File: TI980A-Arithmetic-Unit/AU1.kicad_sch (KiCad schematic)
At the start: 245 parts, among them J1 Circuit Type Test, J2 Circuit Type Test, U1 7413N, U10 74H04N, U100 7410N, U101 7474N, U102 74H52N, U103 74163, U104 7408N, U105 74H11N, U106 74H52N, U107 7451N, U108 74H52N, U109 7404N, U11 74H04N, U110 74H11N, U111 7410N, U112 7420N, U113 7400N, U114 74H54W, U115 7410N, U116 74H11N, U117 74H04N, U118 74H21N, U119 74H52N, U12 74LS74, U120 74188N, U121 74H11N, U122 74157N, U123 7404N, U124 74H11N, U125 74H51N, U126 74H01N, U127 7410N, U128 7474N, U129 7400N, U13 74H00N, U130 74H01N, U131 74H52N, U132 74H05N, U133 74H22N, U134 7410N, U135 7451N, U136 7420N, U137 7427N, U138 74S22N, U139 74S65N, U14 74H10, U140 74H52N, U141 74H52N, U142 74175N, U143 74175N, U144 74H52N, U145 74187, U146 74187, U147 74H52N, U148 74H61N, U149 74H61N, U150 74H61N, U151 7451N, U152 74H61N, U153 74S22N, U154 74H30N, U155 74187, U156 74H04N, U157 74187, U158 74H61N, U159 74H61N, U160 7451N, U161 74H61N, U162 74H61N, U163 74H61N, U164 74H61N, U165 74LS83, U166 74H30N, U167 74H11N, U168 7402N, U169 74H103N, U170 7400N, U171 7402N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

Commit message: Finished Adding Every Chip and Net label in AU1
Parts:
- removed U36: 7402N, symbol 74xx:7402
- removed U76: 7410N, symbol 74xx:74LS10
- added C3, C4: C_Polarized, symbol Device:C_Polarized
- added R49, R50, R51, R52, R54, R55, R56, R73, R74, R75, R76, R78, R79, R80: R, symbol Device:R
- added R53, R77: ~, symbol Device:R
- added U185, U187, U203, U207, U213, U226, U227: 7404N, symbol 74xx:74LS04
- added U186: 74154, symbol 74xx_IEEE:74154
- added U188, U202: 7402N, symbol 74xx:7402
- added U189, U190, U212: 7474N, symbol 74xx:74LS74
- added U191, U204, U217, U218, U220, U224: 7400N, symbol 74xx:7400
- added U192, U199, U208: 7430N, symbol 74xx:74LS30
- added U193, U210, U216, U225: 7420N, symbol 74xx:74LS20
- added U194, U195: 74H21N, symbol 74xx:74LS21
- added U196, U197, U205, U209, U211: 74H54W, symbol TI980A:74H54N
- added U198, U200: 7410N, symbol 74xx:74LS10
- added U201, U36: 74S22N, symbol 74xx:74LS22
- added U206: 7451N, symbol TI980A:7451N
- added U214: 7486N, symbol 74xx:74LS86
- added U215: 74S65N, symbol TI980A:74S65N
- added U219, U221, U223: 74H52N, symbol TI980A:74H52N
- added U222: 7408N, symbol 74xx:74LS08
- added U228: 74S10N, symbol 74xx:74LS10
- added U76: 74H00N, symbol 74xx:7400
- R11: Location AU1 Column 10 Row 05 -> AU1 Col 10 Row 05
- R17, R18, R20, R24, R25: Location AU1 Column 2 Row 09 -> AU1 Col 2 Row 09
- R23: Location AU1 Column 3 Row 01 -> AU1 Col 3 Row 01
- R36: Location AU1 Column 4 Row 12 -> AU1 Col 4 Row 12
- U89: Location AU1 COlumn 13 Row 13 -> AU1 Column 13 Row 13
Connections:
- net AR0XAR2 is gone; now on net ~{AR0XAR2}: U83.11
- net C8OP is gone; now on net C80P: R12.2, U105.1
- net MBL3PA1 is gone; now on net M8L3PA1: U98.13
- net MBl2J2 is gone; now on net MBL2J2: U116.8
- net MCL4P4 is gone; now on net MCL4PA: U124.12
- net ~{AR14XIR9} is gone; now on net ~{AP14XIR9}: U109.6
- net ~{INTRTOPA} is gone; now on net ~{INSRTOPA}: R35.2
- net ~{M8LCPA} is gone; now on net ~{MBLCPA}: U111.8
- net ~{M8LEJ2} is gone; now on net ~{M8LEJ1}: U86.6
- net ~{MAL8AA} is gone; now on net ~{MAL8APA}: U129.3
- net ~{MEM0A} is gone; now on net ~{MEM0}: U24.13
- net ~{ST5T} is gone; now on net ST5T: U109.2
- net A0XA1: now also U207.13
- net ADRV: now also U227.4
- net AL0E1U0: now also U51.6
- net ALU0T: now also U182.9, U51.3, U91.9, U215.4, U36.4
- net ALUEQ8K: now also U182.2
- net AR0: now also U214.1, U215.11
- net AR0XAR1: now also U206.10
- net AR1: now also U214.13
- net AR15: now also U217.9
- net AR1XIR9: now also U214.11
- net AU2CLK: now also U75.9; no longer U21.9
- net BFR0: now also U182.5
- net BFR6: now also U52.3
- net C80P: now also U4.4, U224.2
- net CFZ: now also U26.4
- net CLKONQ: now also U51.9
- net CYCOMP: now also U228.5
- net DMAQ: now also U212.9 (Q)
- net DMARECD: now also U195.8
- net ECEK: now also U58.10
- net ENPCOUT: now also U11.13
- net ER1: now also U51.4, U91.10
- net ER14: now also U194.12
- net ER15: now also U11.11
- net EXEJ: now also U58.4
- net EXPQ: now also U181.9 (Q)
- net EXRCEQ: now also U181.5 (Q)
- net EXRECD: now also U181.2 (D)
- net FCLKT: now also U23.11, U24.6; no longer U23.10, U23.6, U24.11, U24.5
- net FORALA: now also U190.2 (D)
- net FORCE00: now also U29.4
- net FSWON: now also U211.1
- net GCLKE:1: now also U76.13, U76.5
- net GND: now also U179.12 (GND), U179.18 (~{E0}), U179.19 (~{E1}), U186.12 (GND), U186.18 (~{E0}), U186.19 (~{E1}), U196.4, U196.5, U196.6, U205.4, U205.5, U205.6, U215.2, U215.3
- net ILLOPA: now also U76.3
- net ILOPQ: now also U195.1
- net IMM: now also U207.10
- net INAQ: now also U11.1
- net INSRTOP: now also U26.10
- net INTINT: now also U64.9, U91.3
- net INTM: now also U29.12
- net INTST: now also U187.3, U188.13
- net IOINT: now also U227.6
- net IR11: now also U48.5
- net IR5: now also U218.9, U228.9
- net IR56BSD: now also U37.4
- net IR8: now also U37.10
- net IR8T: now also U208.2
- net IR911: now also U48.6, U215.9
- net IR9T: now also U48.4, U213.9, U214.12, U214.2
- net L0: now also U203.4, U211.13, U217.10, U222.13
- net L1: now also U44.2, U197.13, U206.13, U206.3, U211.6, U218.13, U220.2
- net L2: now also U21.3, U193.13, U197.3, U198.13, U222.5, U228.4
- net L23: now also U204.3
- net L2467: now also U225.6
- net L3: now also U184.13, U29.10, U195.13, U197.10, U211.3
- net L4: now also U3.8, U69.11, U74.11, U193.5, U194.13, U197.6, U200.13, U222.2, U224.13
- net L5: now also U185.12, U206.4, U206.9, U209.13, U210.5, U211.10
- net L56: now also U64.6
- net L567: now also U37.9
- net L6: now also U184.5, U200.11, U207.6, U209.3
- net L7: now also U207.4, U209.10, U210.13, U218.10, U224.5
- net L8: now also U209.6
- net L8A: now also U204.8
- net L9: now also U50.5, U77.5, U187.12
- net L9D: now also U77.3
- net LA: now also U185.8
- net LB: now also U200.5, U203.12
- net LC: now also U213.12, U220.10
- net LD: now also U176.4
- net LE: now also U37.5, U185.6, U228.11
- net LF: now also U187.10, U195.5, U196.9
- net M0: now also U75.6, U195.12, U196.13, U196.2, U221.3, U223.3
- net M0L0J3: now also U223.4
- net M0OP: now also U196.1
- net M1: now also U176.10, U221.12, U223.12
- net M3: now also U220.1, U223.1
- net M3L1CJ3: now also U223.2
- net M3L567J1: now also U37.8
- net M5: now also U176.12, U219.3, U221.10
- net M67910: now also U4.1
- net M7: now also U187.8, U196.10
- net M7L3: now also U188.10
- net M8: now also U75.3, U205.10, U221.1
- net M8LB: now also U178.1, U201.9
- net M8LBC: now also U91.13
- net MA: now also U21.8, U219.12
- net MALEFJ3: now also U219.13
- net MB: now also U203.2, U219.10
- net MC: now also U203.10, U228.3
- net MCJ1: now also U224.8
- net MCL3: now also U183.13
- net MD: now also U185.2, U205.3
- net MDJ1: now also U199.8
- net MDPA1: now also U192.8
- net ME: now also U176.8, U44.1
- net MEL3: now also U202.4
- net MEM0PA1: now also U113.8; no longer U98.4
- net MEM10A: now also U24.10
- net MEM12: now also U26.6, U228.2
- net MEM5A: now also U4.2, U198.3
- net MEM6: now also U23.5
- net MEM6A: now also U198.4
- net MEM7A: now also U198.5
- net MEM8A: now also U29.6, U220.9
- net MFLC: now also U188.1
- net MFM0PA1: now also U98.4; no longer U113.8
- net MRESETQ: now also U222.12
- net R22: now also U216.10
- net RAC0: now also U186.20 (A3)
- net RAC1: now also U186.21 (A2)
- net RAC2: now also U186.22 (A1)
- net RAC3: now also U186.23 (A0)
- net RAC4: now also U179.20 (A3)
- net RAC5: now also U179.21 (A2)
- net RAC6: now also U179.22 (A1)
- net RAC7: now also U179.23 (A0)
- net RDYIO: now also U227.10
- net RR: now also U228.1
- net RUNFFQ: now also U50.1, U197.1, U216.12
- net SC0: now also U91.2, U213.1
- net SC2: now also U48.10
- net SC3: now also U48.9, U222.9
- net SC3B: now also U222.8
- net SCNT06: now also U48.8
- net SCNT0F: now also U220.5
- net SCNT1E: now also U222.1, U222.4
- net SELBFR: now also U52.2
- net SELBFRB: now also U224.1
- net SELBFRC: now also U183.9, U76.4
- net SELJ3: now also U183.6
- net SELJ3A: now also U223.8
- net SELJ3B: now also U219.8
- net SELPAA: now also U221.8
- net TRP13Q: now also U195.9, U212.5 (Q)
- net TRP1413: now also U52.12
- net TRP14Q: now also U189.9 (Q), U195.2
- net UR0: now also U51.5, U91.11, U213.3
- net VCC1: now also U179.24 (VCC), U180.11, U180.12, U180.6, U181.1 (~{R}), U181.10 (~{S}), U181.13 (~{R}), U181.4 (~{S}), U183.10, U183.4, U21.2, U3.10, U52.1, U75.10, U75.2, U75.5, U77.12, U91.5, C3.1, C4.1, R49.1, R50.1, R51.1, R52.1, R53.1, R54.1, R55.1, R56.1, R73.1, R74.1, R75.1, R76.1, R77.1, R78.1, R79.1, R80.1, U186.24 (VCC), U189.1 (~{R}), U189.10 (~{S}), U189.13 (~{R}), U189.4 (~{S}), U190.1 (~{R}), U190.4 (~{S}), U191.1, U197.4, U199.12, U208.11, U209.4, U212.1 (~{R}), U212.10 (~{S}), U212.13 (~{R}), U212.4 (~{S}), U215.13, U219.5, U221.5, U222.10, U223.5
- net XRDSW: now also U45.6, U209.5
- net ~{A0XA1}: now also U74.9, U207.12
- net ~{ADRV}: now also U227.3
- net ~{ALU0T}: now also U182.8, U201.12, U201.4, U215.1
- net ~{ALUEQ8K}: now also U182.1
- net ~{AR0T}: now also U215.5
- net ~{ARDSW}: now also U184.10, U47.3
- net ~{ARESW}: now also U184.9, U207.1
- net ~{BFR0}: now also U182.6
- net ~{BRDSW}: now also U45.11, R50.2, U193.1, U200.1
- net ~{BRESW}: now also U184.12
- net ~{CLCNT}: now also U225.8
- net ~{CNT}: now also U225.10
- net ~{DEVTHERE}: now also U183.1
- net ~{DMAINT}: now also R75.2, U226.13
- net ~{DMAM}: now also U204.12, U216.2
- net ~{E14XE15}: now also U69.9
- net ~{ENAPI1}: now also U228.6
- net ~{ENIOUT}: now also U51.8
- net ~{ENPCOUT}: now also U11.12, U51.10
- net ~{ERDSW}: now also R54.2, U193.2
- net ~{ERESW}: now also U47.5, R56.2, U193.4
- net ~{EXPINT}: now also U47.13
- net ~{EXPM}: now also U194.4, U216.1
- net ~{FCLKT}: now also U24.5; no longer U23.5, U24.6
- net ~{FORCE00}: now also U183.3, U183.5, U29.3
- net ~{GCLKF:1}: now also U190.3 (C)
- net ~{GCLKF:2}: now also U181.11 (C), U181.3 (C), U189.3 (C)
- net ~{GCLKF:3}: now also U75.8; no longer U21.8
- net ~{IAQBFR}: now also U216.8
- net ~{IFLAGQ}: now also U91.4
- net ~{INAQ}: now also U11.2, U64.10, U194.1, U216.5, U76.10
- net ~{INSRTOPA}: now also U26.8
- net ~{INTABORT}: now also U226.9
- net ~{INTM}: now also U29.13, U216.13
- net ~{IOINT}: now also R76.2, U227.5
- net ~{IOM}: now also U203.5, U204.13
- net ~{IR10}: now also U208.12
- net ~{IR5T}: now also U208.5
- net ~{IR6T}: now also U208.4, U228.10
- net ~{IR7T}: now also U208.3
- net ~{IR9T}: now also U205.13, U208.1, U213.8
- net ~{IRDSW}: now also U45.9, R51.2, U193.9, U198.1
- net ~{L01}: now also U58.6
- net ~{L0}: now also U179.1 (~{S0}), U74.4, U203.3
- net ~{L1}: now also U179.2 (~{S1}), U58.9
- net ~{L2}: now also U179.3 (~{S2}), U180.1, U21.1, U204.1, U225.1
- net ~{L3}: now also U179.4 (~{S3}), U180.2, U29.11, U188.9, U202.6, U204.2
- net ~{L4}: now also U178.6, U179.5 (~{S4}), U180.3, U3.9, U69.1, U74.5, U225.4
- net ~{L5}: now also U179.6 (~{S5}), U180.4, U64.5, U69.2, U185.13
- net ~{L6}: now also U179.7 (~{S6}), U180.5, U64.4, U69.13, U207.5, U225.2
- net ~{L7}: now also U179.8 (~{S7}), U207.3, U225.5
- net ~{L8}: now also U179.9 (~{S8}), U188.6, U204.9, U217.1
- net ~{LA}: now also U179.11 (~{S10}), U185.9, U204.10, U204.4
- net ~{LB}: now also U178.2, U179.13 (~{S11}), U202.12, U203.13, U204.5
- net ~{LC}: now also U179.14 (~{S12}), U58.3, U188.3, U213.13
- net ~{LDSC}: now also U224.3, U225.9
- net ~{LE}: now also U178.12, U179.16 (~{S14}), U185.5, U217.2
- net ~{LF}: now also U179.17 (~{S15}), U187.11, U188.12
- net ~{LRACLR}: now also U44.3
- net ~{LRDSW}: now also R77.2, U210.2, U227.13
- net ~{LRESW}: now also R52.2, U210.1, U226.1
- net ~{M0L4BFR}: now also U77.11
- net ~{M0LEJ1}: now also U228.8
- net ~{M0}: now also U178.5, U75.4, U186.1 (~{S0})
- net ~{M1}: now also U176.11, U186.2 (~{S1})
- net ~{M2}: now also U186.3 (~{S2}), U203.9
- net ~{M3}: now also U186.4 (~{S3})
- net ~{M4}: now also U186.5 (~{S4})
- net ~{M5L2PA}: now also U217.5
- net ~{M5}: now also U176.13, U186.6 (~{S5})
- net ~{M6}: now also U186.7 (~{S6}), U202.11
- net ~{M8L0J1}: now also U217.8
- net ~{M8L2PA}: now also U220.12
- net ~{M8L456J1}: now also U202.1
- net ~{M8LEJ1}: now also U218.5
- net ~{M8}: now also U178.3, U58.2, U186.9 (~{S8})
- net ~{MAESW}: now also U47.1
- net ~{MALCPA1}: now also U220.8
- net ~{MALEBFR}: now also U50.12
- net ~{MA}: now also U178.11, U21.9, U186.11 (~{S10}), U216.9
- net ~{MBL6CJ3}: now also U213.5
- net ~{MBLA8PA}: now also U218.3
- net ~{MB}: now also U178.8, U186.13 (~{S11}), U203.1
- net ~{MCLDJ1}: now also U224.10
- net ~{MC}: now also U186.14 (~{S12}), U203.11
- net ~{MDDSW}: now also U45.3, R55.2, U191.4
- net ~{MDESW}: now also U44.4
- net ~{MDIDSW}: now also U191.5
- net ~{MDIESW}: now also U44.5
- net ~{MDL1PA1}: now also U192.1
- net ~{MDL8PA1}: now also U192.12
- net ~{MD}: now also U58.8, U185.1, U186.15 (~{S13})
- net ~{MEM10}: now also U24.11
- net ~{MEM11}: now also U187.1
- net ~{MEM15}: now also U226.5
- net ~{MEM6}: now also U23.6
- net ~{MEM8}: now also U29.5
- net ~{ME}: now also U176.9, U58.5, U186.16 (~{S14}), U202.5
- net ~{MF}: now also U186.17 (~{S15}), U187.5, U188.11, U188.2, U188.5
- net ~{MRDSW}: now also U184.1, U191.2
- net ~{MRESW}: now also R80.2, U210.4
- net ~{OVRST}: now also U208.8
- net ~{PCDSW}: now also R49.2, U193.10
- net ~{PCESW}: now also U45.13, U193.12
- net ~{R19}: now also U51.11
- net ~{RDYIO}: now also R74.2, U227.11
- net ~{RRDESZ}: now also U26.5, U228.13
- net ~{RSTSW}: now also U227.1
- net ~{RUNFFQ}: now also U211.4
- net ~{SCNT0F}: now also U69.10, U194.9
- net ~{SCNT1E}: now also U74.10, U74.3, U218.12, U218.2
- net ~{SELBFRCK}: now also U76.6
- net ~{SELJ1}: now also U215.8
- net ~{SELJ2B}: now also U205.8
- net ~{SELJ2C}: now also U91.12
- net ~{SELJ3}: now also U183.2
- net ~{SELOP}: now also U196.8
- net ~{SELPA}: now also U201.6, U201.8, U36.6
- net ~{SRDSW}: now also R73.2, U210.10, U226.3
- net ~{SRESW}: now also R78.2, U210.9, U226.11
- net ~{STDSW}: now also U184.2
- net ~{STESW}: now also U184.4, U47.9
- net ~{STRTSW}: now also R53.2
- net ~{SYSCLK}: now also U23.10; no longer U23.11, U24.10
- net ~{T2OR6}: now also U176.2
- net ~{T4OR6}: now also U176.6
- net ~{TRP13}: now also U195.4
- net ~{UR0T}: now also U201.5, U213.11, U213.4
- net ~{XRDSW}: now also U45.5, U200.3
- net ~{XRESW}: now also R79.2, U210.12
- net EXPINT: now reaches U181.12 (D)
- net EXPINT: now also U47.12
- net ~{EXPQ}: now reaches U181.8 (~{Q})
- net M0LEOP: now reaches U37.6
- net M0LEOP: now also U196.3
- net M8LC: now reaches U58.1
- net M8LC: now also U201.1, U36.1
- net T4OP6: now reaches U176.5
- net T4OP6: now also U194.6, U212.2 (D)
- net ~{ER15T}: now reaches U11.10
- net ~{ER15T}: now also U194.10
- net ~{M8L4PA}: now reaches U69.8
- net ~{M8L4PA}: now also U220.13
- net ~{M1L4PA}: now reaches U74.8
- net ~{M1L4PA}: now also U191.9
- net ~{MDL3PA1}: now reaches U184.8
- net ~{MDL3PA1}: now also U192.3
- net ERESW: now reaches U47.6
- net ERESW: now also U200.2
- net L456: now reaches U69.12
- net L456: now also U220.4
- net ~{AL0E1U0}: now reaches U91.8
- net ~{AL0E1U0}: now also U91.1
- net M0L4: now reaches U178.4
- net M0L4: now also U77.13
- net ~{MDL6PA1}: now reaches U184.6
- net ~{MDL6PA1}: now also U192.6
- net ~{INTINT}: now reaches U91.6
- net ~{INTINT}: now also U50.2, U194.2
- net MDE: now reaches U44.6
- net MDE: now also U77.4, U185.3
- net ~{MDL9J2}: now reaches U77.6
- net ~{MDL9J2}: now also U198.11
- net ~{LD}: now reaches U176.3
- net ~{LD}: now also U178.9, U179.15 (~{S13}), U77.2
- net MEM11A: now reaches U4.5
- net MEM11A: now also U187.2
- net ~{ILLSKIP}: now reaches U4.6
- net ~{ILLSKIP}: now also U76.2
- net T20R6: now reaches U176.1
- net T20R6: now also U189.12 (D), U217.11
- net MBLD: now reaches U178.10
- net MALE: now reaches U178.13
- net MALE: now also U50.13
- net ~{IMM}: now reaches U26.9
- net ~{IMM}: now also U198.6, U207.11
- net ARDSW: now reaches U47.4
- net ARDSW: now also U211.2
- net STESW: now reaches U47.8
- net STESW: now also U200.10
- net at U138.2, U62.13: now also U201.10, U201.2, U213.2, U36.2
- net ~{MDE}: now reaches U50.3
- net ~{MDE}: now also U185.4
- net MDDID: now reaches U50.4
- net MDDID: now also U191.6
- net ~{MDL9J1}: now reaches U50.6
- net ~{MDL9J1}: now also U199.11
- net L23456: now reaches U180.8
- net MDDSW: now reaches U45.4
- net ~{ILOPD}: now reaches U183.8
- net ~{ILOPD}: now also U29.9
- net ~{M1PAA}: now reaches U74.6
- net ~{M1PAA}: now also U191.10
- net MAESW: now reaches U47.2
- net MAESW: now also U200.4
- net PCESW: now reaches U45.12
- net PCESW: now also U198.2
- net ILOPD: now reaches U29.8
- net ILOPD: now also U189.2 (D)
- net ~{L9}: now reaches U179.10 (~{S9})
- net ~{L9}: now also U77.1, U187.13
- net BRDSW: now reaches U45.10
- net BRDSW: now also U197.5
- net ~{EXRECQ}: now reaches U181.6 (~{Q})
- net ~{INT14A}: now reaches U64.8
- net ~{INT14A}: now also U217.12
- net ~{M9}: now reaches U75.1
- net ~{M9}: now also U185.11, U186.10 (~{S9})
- net IRDSW: now reaches U45.8
- net IRDSW: now also U197.2
- net L8F renamed L8E
- net L8E: now also U217.3
- new net AR0XIR9: U206.1, U214.3
- new net ARESW: U197.9, U207.2
- new net DMAINT: U212.12 (D), U226.12
- new net DMAIO: U194.5, U204.11
- new net FORALAQ: U190.5 (Q), U208.6
- new net GND1: C3.2, C4.2
- new net INOPQ: U189.5 (Q)
- new net INTABORT: U224.12, U226.8
- new net INTIAQ: U76.12, U76.8
- new net IOM: U203.6, U216.4
- new net LAB: U204.6, U218.1
- new net LRDSW: U211.9, U227.12
- new net LRESW: U209.1, U226.2
- new net M0L0PA: U221.4, U222.11
- new net M1L4J3: U222.3, U223.13
- new net M1PA: U191.8, U221.13
- new net M2: U203.8, U206.2, U206.5, U223.10
- new net M2L15J3: U207.8, U223.11
- new net M5L12PA: U217.6, U221.11
- new net M5L2J3: U219.4, U222.6
- new net M6LB: U202.13, U215.12, U215.6
- new net M8J2: U205.9, U218.6
- new net M8L24PA: U220.11, U221.2
- new net M8L4J1: U194.8, U202.2
- new net M8L56J1: U202.3
- new net M9: U185.10
- new net MBL6CJ3: U213.6, U219.11
- new net MDJ2: U198.8, U205.2
- new net MEM15A: U226.6
- new net MF: U187.6, U219.1
- new net MFL8: U188.4, U205.1, U215.10
- new net MFLFJ3: U195.6, U219.2
- new net MRDSW: U191.3, U209.2
- new net RSTSW: U211.5, U227.2
- new net SRDSW: U224.4, U226.4
- new net SRESW: U209.9, U226.10
- new net UR0T: U201.13, U213.10, U36.5
- new net ~{DMAQ}: U212.8 (~{Q})
- new net ~{FORALAQ}: U190.6 (~{Q})
- new net ~{GCLHF:3}: U212.11 (C)
- new net ~{INOPQ}: U189.6 (~{Q})
- new net ~{INT14B}: U216.6, U217.13
- new net ~{INTST}: U187.4, U76.9
- new net ~{M2L15J3}: U206.8, U207.9
- new net ~{M2L15}: U206.6, U225.12
- new net ~{M3L1}: U220.3, U225.13
- new net ~{M5L1PA}: U217.4, U218.11
- new net ~{M7}: U186.8 (~{S7}), U187.9, U188.8
- new net ~{M8J2A}: U218.4, U220.6
- new net ~{MCL4J1}: U224.11, U224.9
- new net ~{MDJ1A}: U199.1, U211.8
- new net ~{MDJ2A}: U197.8, U198.9
- new net ~{MDJ2B}: U198.10, U209.8
- new net ~{MDL2J1}: U198.12, U199.2
- new net ~{MDL2PA1}: U192.2, U193.8
- new net ~{MDL4J1}: U199.3, U200.12
- new net ~{MDL4PA1}: U192.4, U193.6
- new net ~{MDL5PA1}: U192.5, U210.6
- new net ~{MDL6J1}: U199.4, U200.8
- new net ~{MDL7J1}: U199.5, U218.8, U224.6
- new net ~{MDL7PA1}: U192.11, U210.8
- new net ~{MDL8J1}: U199.6, U200.6
- new net ~{RRILLOP}: U228.12, U76.1
- new net ~{TRP13Q}: U212.6 (~{Q})
- new net ~{TRP14Q}: U189.8 (~{Q}), U195.10
- new net ~{TRPCLK}: U189.11 (C), U212.3 (C), U76.11
- no-connect marks 161 -> 195
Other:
- note added: "BFR(0-7) Signals Used as Next ROM Address for SELBFR"
- note added: "BFR0 = BFR0 ROM Output"
- note added: "Basic Function ROM (BFR) The 32x8 Word Rom in the BFR Logic Decodes Bsic Information about an Instruction Being Fetched"
- note added: "Branch, Store or Double Instuction Flag"
- note added: "Clock Enabled During SELBFR"
- note added: "DBL"
- note added: "Denotes Byte Inst. In Process"
- note added: "Double Length Instruction Flag"
- note added: "Expansion Interrupt Recognized"
- note added: "Forces BFR(4-7) to Zero for Shift Inst. with C Field=0"
- note added: "INTERUPT LOGIC"
- note added: "IXB Field = 111"
- note added: "Illegal OP Code Flag"
- note added: "Illegal Skip or RR Instruction"
- note added: "MEMORY DATA BUFFERING"
- note added: "Masked DMA Interrupt"
- note added: "Masked I/O Interrupt"
- note added: "Next ROM Address Selector Select J2 (~{SELJ2})"
- note added: "RR Instruction with Illegal Destination"
- note added: "RR Interrupt Inhibit (When DEST = ST)"
- note added: "Select J3 as Next ROM Address (SELJ3)"
- note added: "Select Present Address + 1 as Next ROM Address (~{SELPA1})"
- note added: "Select Present ROM Address as the Next ROM Address"
- note added: "Syncronized DMA Interrupt"
- note added: "Syncronized I/O Interrupt"
- note added: "Transfer MEM(024) to BFR(3-7)"
- note added: "Trap Address Identification FF"
- note added: "Unused Gates"
- moved on the sheet: R22, R28, R29, R33, R34, R35

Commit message: Finished AU1 Schematic
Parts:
- removed R14, R40, R44, R75, R76: R, symbol Device:R
- removed R22: ~, symbol Device:R
- removed unit 3 of U121
- removed unit 3 of U13
- removed U154, U166: 74H30N, symbol 74xx:74LS30
- removed unit 2 of U167
- removed U168: 7402N, symbol 74xx:7402
- removed U169: 74H103N, symbol TI980A:74H103N
- removed U170: 7400N, symbol 74xx:7400
- removed unit 1 of U171
- removed unit 3 of U171
- removed unit 3 of U176
- removed unit 1 of U176
- removed U180: 7430N, symbol 74xx:74LS30
- removed U181, U212, U80: 7474N, symbol 74xx:74LS74
- removed unit 2 of U187
- removed unit 4 of U188
- removed unit 2 of U189
- removed unit 1 of U194
- removed unit 2 of U195
- removed unit 3 of U203
- removed unit 4 of U204
- removed unit 1 of U216
- removed unit 4 of U217
- removed unit 4 of U22
- removed unit 6 of U226
- removed unit 3 of U227
- removed unit 1 of U27
- removed unit 1 of U35
- removed unit 6 of U47
- removed unit 2 of U56
- removed unit 3 of U64
- removed unit 4 of U76
- removed unit 3 of U76
- removed unit 6 of U8
- removed U81: 74H54W, symbol TI980A:74H54N
- removed unit 2 of U84
- removed unit 1 of U84
- removed unit 3 of U86
- removed unit 2 of U90
- added U229: 7402N, symbol 74xx:7402
- R57, R59: Location AU1 Column 2 Row 09 -> AU1 Col 2 Row 09
- R58, R60, R65, R66, R68, R70, R71, R72: Location AU1 Column 3 Row 18 -> AU1 Col 3 Row 18
- R61: Location AU1 Column 3 Row 01 -> AU1 Col 3 Row 01
- R62, R63, R64, R67, R69: Location AU1 Column 4 Row 12 -> AU1 Col 4 Row 12
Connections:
- net ADRB is gone; now on net ADRV: U82.12
- net M8L5J1 is gone; now on net M8L56J1: U110.12
- net MBLD is gone; now on net M8LD: U178.10
- net MFM0PA1 is gone; now on net MEM0PA1: U98.4
- net STO1 is gone; now on net ST01: U85.3
- net ~{IR56BSD} is gone; now on net IR56BSD: U137.8
- net ~{MAL0RDYQ} is gone; now on net ~{MALDRDYQ}: U85.9
- net ~{MALEBFR} is gone; now on net ~{M0L4BFR}: U167.2, U50.12, U56.10
- net ~{PF1Q} is gone; now on net PF1Q: U49.8 (~{Q}), U52.4
- net ~{ST0T} is gone; now on net ~{STOT}: U123.8
- net AR14: no longer U82.10
- net EXTFORMA: now also U229.4; no longer U87.2, U87.4, U87.5
- net EXTFORMB: now also U87.2
- net FORCE00: now also U183.5
- net INTM: now also U82.10
- net IR12T: now also U229.2
- net IR13: now also U229.3
- net IR14T: now also U229.11
- net IR15T: now also U229.12
- net IR8: now also U229.5
- net IR8T: now also U117.4; no longer U117.3
- net IR9T: now also U229.6
- net M0L8BEJ2: no longer U114.1
- net M1L8: now also U229.10
- net ~{FORCE00}: no longer U183.5
- net ~{IR8}: now also U117.3; no longer U117.4
- net ~{L8}: now also U229.9
- net ~{M0L7J1}: now also U218.8
- net ~{M0L8J1}: no longer U84.8
- net ~{M0LBJ1}: now also U84.8
- net ~{M1}: now also U229.8
- net ~{M8LEJ1}: no longer U218.5, U86.6
- net ~{M8}: now also U178.8, U75.1
- net ~{M9}: no longer U75.1
- net ~{MB}: no longer U178.8
- net ~{MDL7J1}: no longer U218.8
- net ~{SC0}: now reaches U138.2, U201.10, U201.2, U213.2, U36.2, U62.13
- new net EXTFORMC: U229.1, U87.4
- new net EXTFORMD: U229.13, U87.5
- new net ~{M8LEJ2}: U218.5, U86.6
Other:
- added sheet Interrupt Logic AU1 (AU1-INT-LOGIC.kicad_sch)
- note added: "(~{SELJ1})"
- note added: "(~{SELOP})"
- note added: "A Register Bit 16 Load Control"
- note added: "A Register Clear Control"
- note added: "ALU Function Selects on AU1 Part of ALU S2 Select Input"
- note added: "Basic Function ROM (BFR) The 32x8 Word Rom in the BFR Logic Decodes Basic Information about an Instruction Being Fetched"
- note added: "Least Significant State Decoder"
- note added: "Mask ROMs to Next ROM Address Selector"
- note added: "Most Significant State Decoder"
- note added: "Next ROM Address"
- note added: "Outputs to AU Interconnect"
- note added: "Outputs to Backplane"
- note added: "PF1Q and PF2Q are Flip-Flops Configured Such that (~{PF1Q} * PF2Q) Indicates the Negative Edge of the PFAIL Pulse."
- note added: "Part of Bus C Select Input A"
- note added: "Part of Bus C Select Input B"
- note added: "Part of ER15SELA"
- note added: "Part of INHLSA Inhibit the Least Significatn 8 Bits of Bus A"
- note added: "Part of MA increment control (for Memory Controller)"
- note added: "Part of Test Logic"
- note added: "Program Counter Increment Control"
- note added: "Pull-Ups"
- note added: "ROM Address Increment"
- note added: "ROM Address Register"
- note added: "Ready Flip-Flop"
- note added: "Special Console Control Logic"
- note added: "TERMIO FLIP-FLOP"
- note added: "Test Connector"
- note added: "To Next ROM Address Selector"
- note added: "~{GOIO} FLIP-FLOP"
- note added: "~{SCER} CT To AU1 AU Interconnect P1 Pin 22 To AU2 AU Interconnect P1 Pin 22"
- note added: "~{ST2CLR} Enables a Clock to Reset ST2 for Arithmetic Zero Shifts"
- note removed: "ALU Function Selects Contrl on AU1"
- note removed: "Basic Function ROM (BFR) The 32x8 Word Rom in the BFR Logic Decodes Bsic Information about an Instruction Being Fetched"
- note removed: "DMAREC CB To XA11 P1 Pin 73 To XA07(AU1) P1 Pin 69"
- note removed: "Denotes Byte Inst. In Process"
- note removed: "Expansion Interrupt Recognized"
- note removed: "INTERUPT LOGIC"
- note removed: "LSB11 Resets the Highest Priority EXP. Interrupt"
- note removed: "Masked DMA Interrupt"
- note removed: "Masked I/O Interrupt"
- note removed: "Masked Memory Parity Error Interrupt"
- note removed: "Masked Optional Expanded Interrupt"
- note removed: "PF1Q and PF2Q are FLip-Flops Configured Such that (~{PF1Q} * PF2Q) Indicates the Negative Edge of the PFAIL Pulse."
- note removed: "Special Console Control"
- note removed: "Status Register"
- note removed: "Synchronized DMA Interrupt Reconized Signal"
- note removed: "Syncronized DMA Interrupt"
- note removed: "Syncronized I/O Interrupt"
- note removed: "Trap Address Identification FF"
- moved on the sheet: C3, C4, CTP1, CTP2, J1, J2, R28, R29, R32, R33, R34, R35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

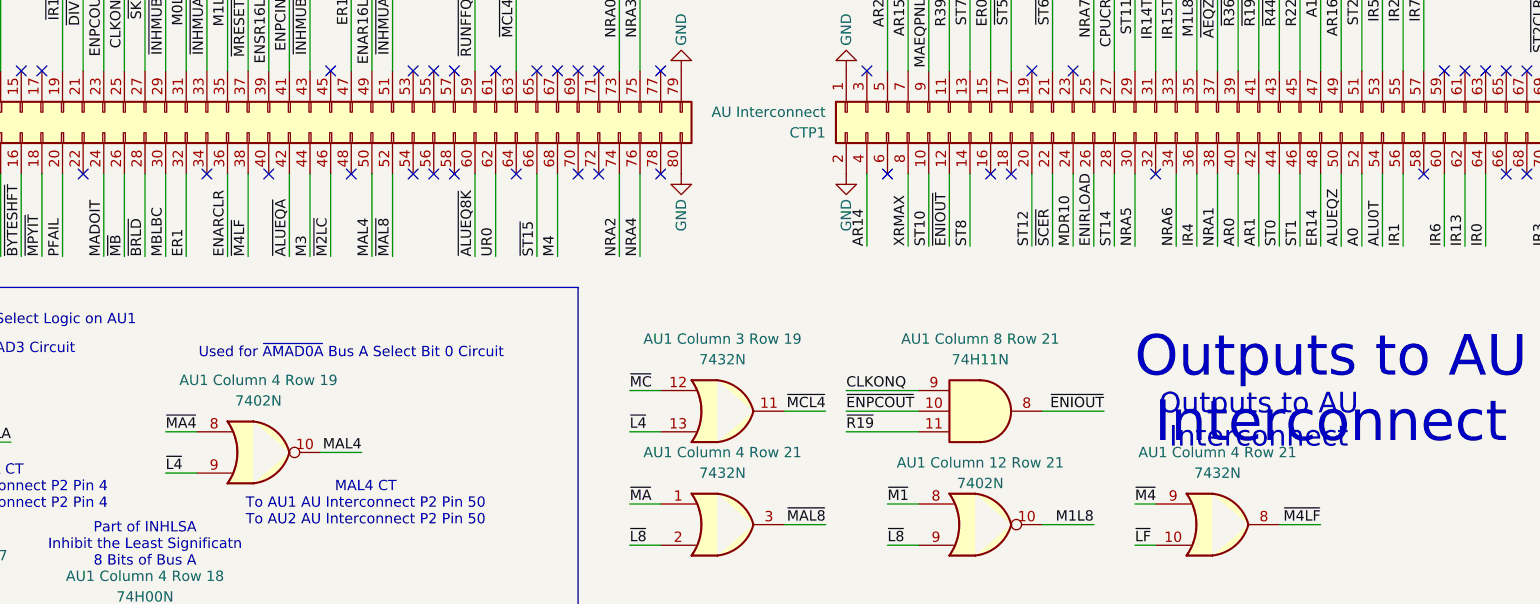
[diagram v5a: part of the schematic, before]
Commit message: Finished Up to Column 3 on AU2
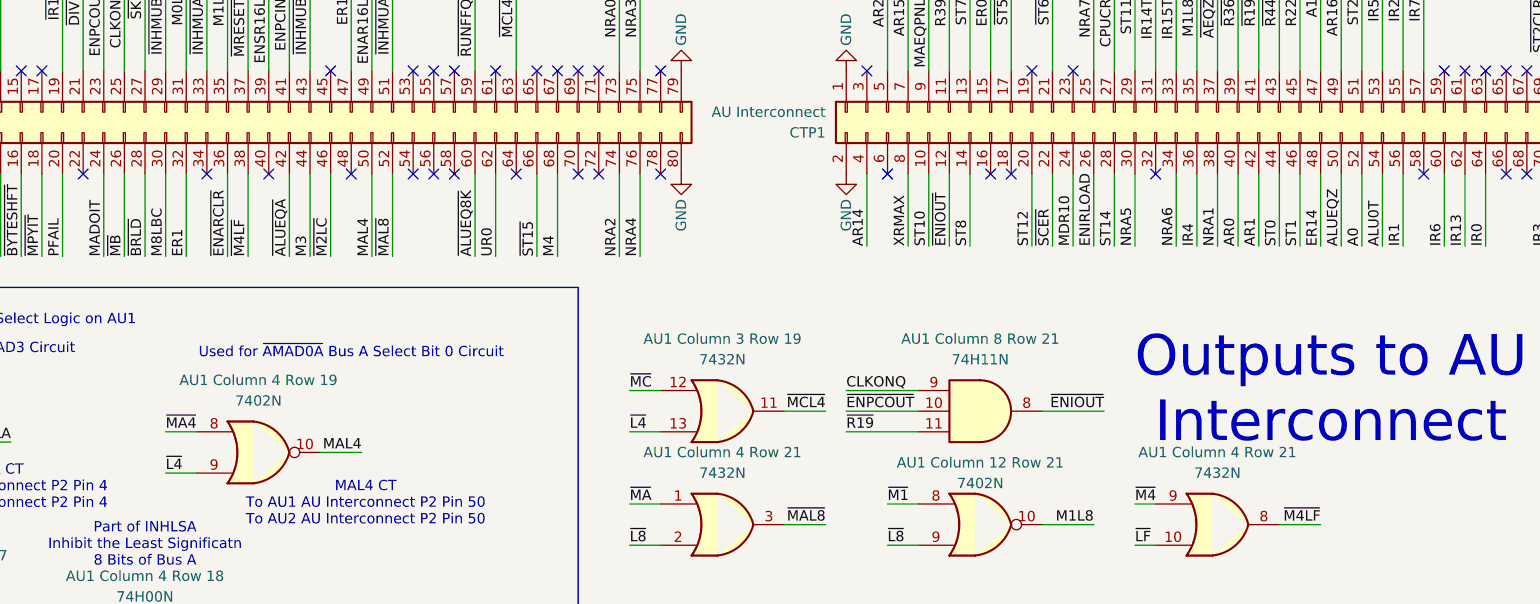
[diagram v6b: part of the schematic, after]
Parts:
- R33, R34, R37, R45, R53, R57, R65, R77: value ~ -> (none)
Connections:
- net ENARCLR is gone; now on net ~{ENARCLR}: CTP2.36 (Pin_36)
- net MBLBC is gone; now on net M8LBC: CTP2.30 (Pin_30)
